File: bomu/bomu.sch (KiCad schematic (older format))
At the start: 15 parts, among them U1 nRF52840

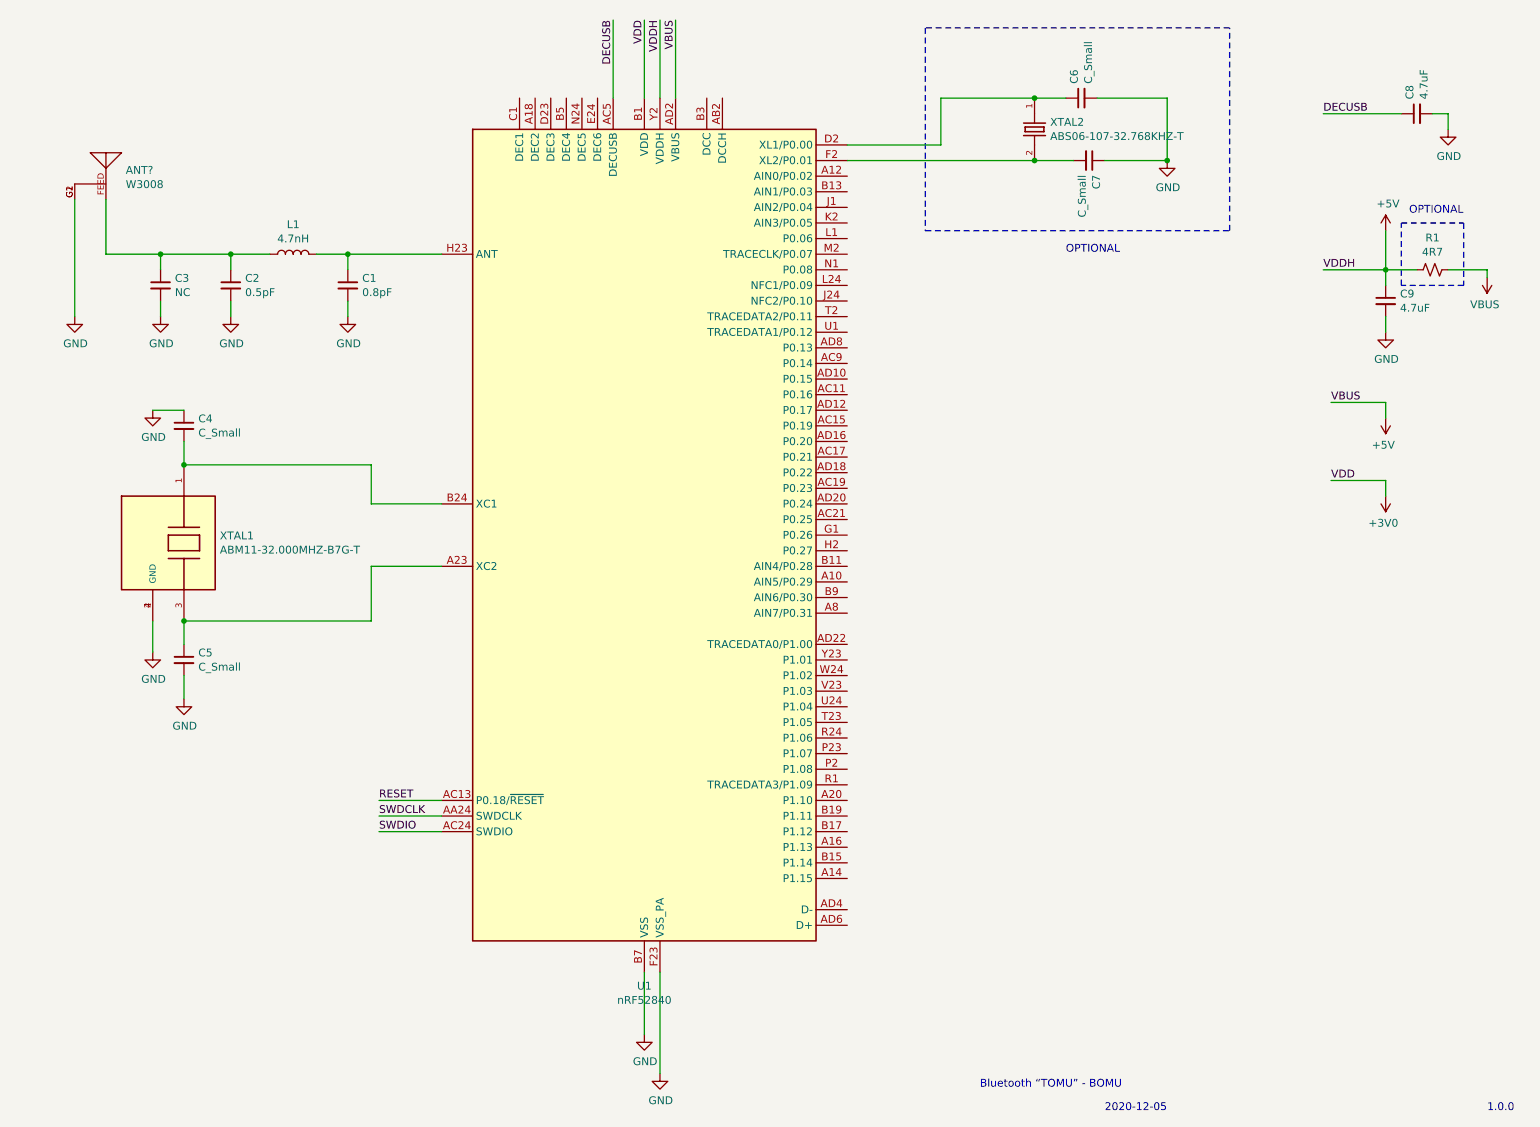
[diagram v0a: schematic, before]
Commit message: Swapped QFN for WLCSP
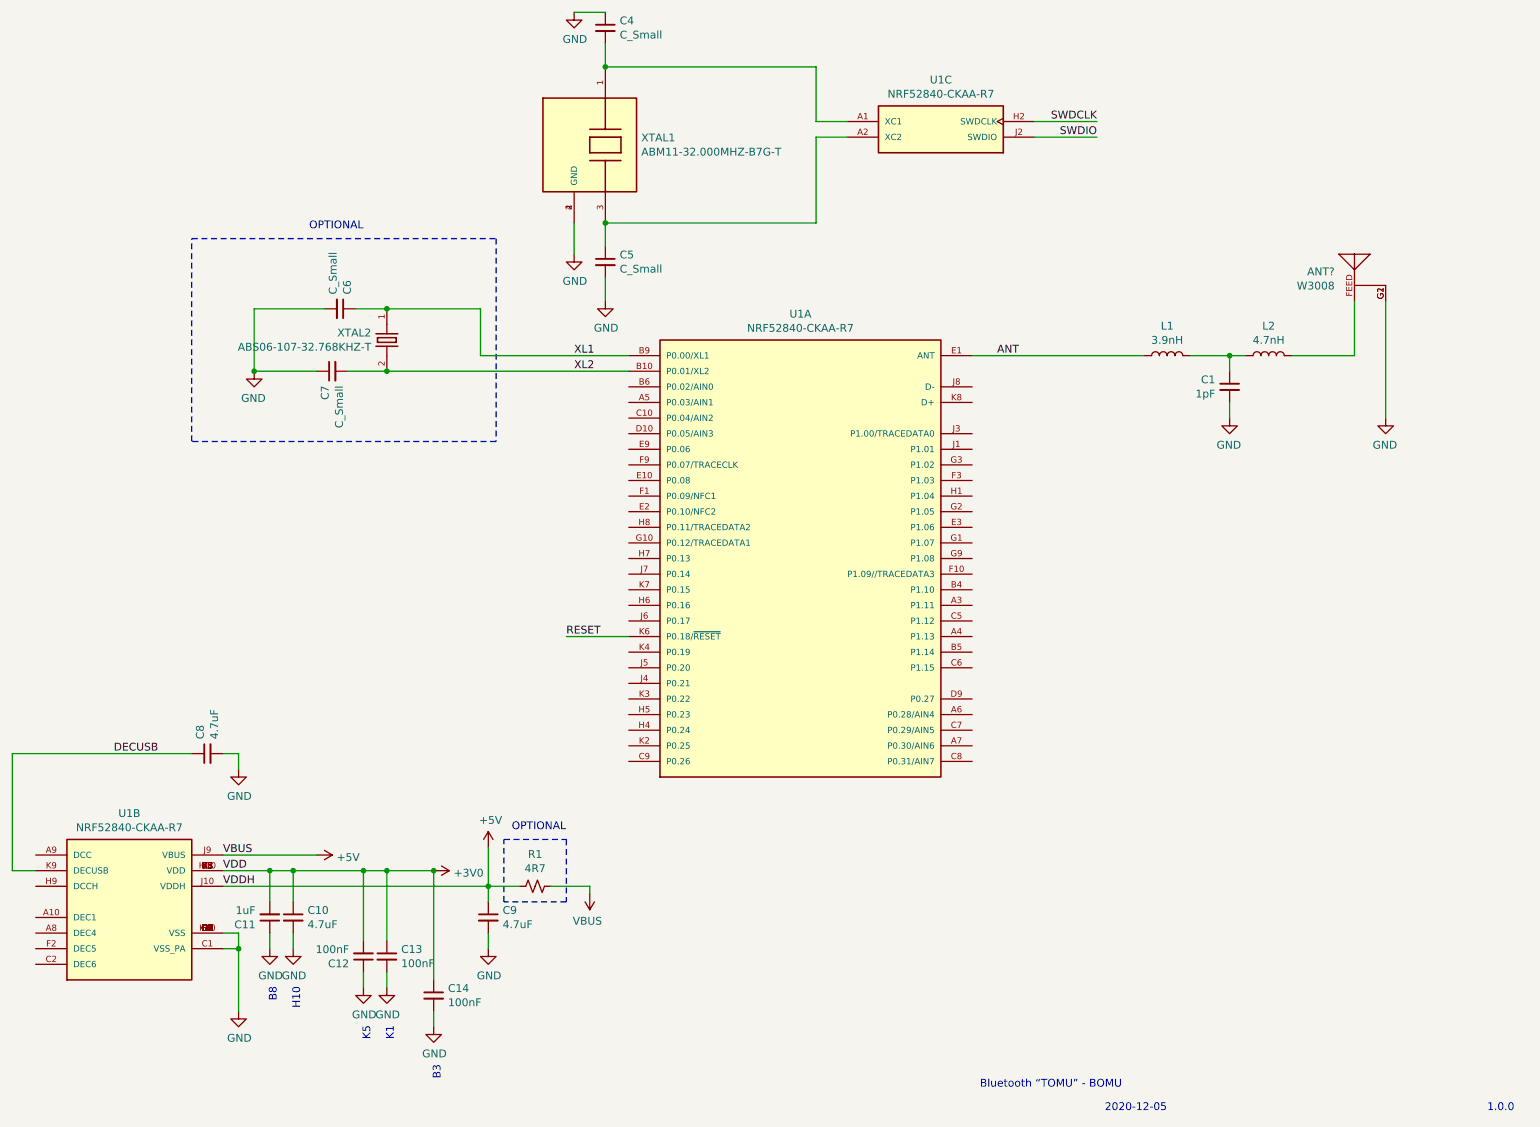
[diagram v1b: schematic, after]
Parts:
- removed C2: 0.5pF, Capacitor_SMD:C_0201_0603Metric, symbol Device:C_Small
- removed C3: NC, Capacitor_SMD:C_0201_0603Metric, symbol Device:C_Small
- removed U1: nRF52840, Package_DFN_QFN:Nordic_AQFN-73-1EP_7x7mm_P0.5mm, symbol MCU_Nordic:nRF52840
- added C10: 4.7uF, Capacitor_SMD:C_0201_0603Metric, symbol Device:C_Small
- added C11: 1uF, Capacitor_SMD:C_0201_0603Metric, symbol Device:C_Small
- added C12, C13, C14: 100nF, Capacitor_SMD:C_0201_0603Metric, symbol Device:C_Small
- added L2: 4.7nH, Inductor_SMD:L_0201_0603Metric, symbol Device:L
- added U1: NRF52840-CKAA-R7, BGA94N35P10X10_360X354X51N, symbol NRF52840-CKAA-R7:NRF52840-CKAA-R7
- C1: value 0.8pF -> 1pF
- L1: value 4.7nH -> 3.9nH
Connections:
- net +3V0: now also C10.1, C11.2, C12.2, C13.1, C14.1, U1.B3 (VDD), U1.B8 (VDD), U1.H10 (VDD), U1.K1 (VDD), U1.K5 (VDD)
- net +5V: now also U1.J10 (VDDH), U1.J9 (VBUS)
- net DECUSB: now also U1.K9 (DECUSB)
- net GND: now also C10.2, C11.1, C12.1, C13.2, C14.2, U1.B7 (VSS), U1.C1 (VSS_PA), U1.C4 (VSS), U1.D3 (VSS), U1.D4 (VSS), U1.D5 (VSS), U1.D6 (VSS), U1.D7 (VSS), U1.D8 (VSS), U1.E4 (VSS), U1.E5 (VSS), U1.E6 (VSS), U1.E7 (VSS), U1.E8 (VSS), U1.F4 (VSS), U1.F5 (VSS), U1.F6 (VSS), U1.F7 (VSS), U1.F8 (VSS), U1.G4 (VSS), U1.G5 (VSS), U1.G6 (VSS), U1.G7 (VSS), U1.G8 (VSS), U1.K10 (VSS)
- net RESET: now also U1.K6 (P0.18/~RESET)
- net SWDCLK: now also U1.H2 (SWDCLK)
- net SWDIO: now also U1.J2 (SWDIO)
- net at C5.1, XTAL1.3: now also U1.A2 (XC2)
- net at C4.2, XTAL1.1: now also U1.A1 (XC1)
- net XL1: now reaches C6.1, XTAL2.1
- net XL1: now also U1.B9 (P0.00/XL1)
- net XL2: now reaches C7.2, XTAL2.2
- net XL2: now also U1.B10 (P0.01/XL2)
- net at C1.1: now also L1.1, L2.2; no longer L1.2
- net at ANT?.FEED: now also L2.1; no longer L1.1
- new net ANT: L1.2, U1.E1 (ANT)
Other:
- note added: "B3"
- note added: "B8"
- note added: "H10"
- note added: "K1"
- note added: "K5"
- moved on the sheet: ANT?, C1, C4, C5, C6, C7, C8, C9, L1, R1, XTAL1, XTAL2
